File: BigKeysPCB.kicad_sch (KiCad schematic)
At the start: 24 parts, among them SW1 SW_Push, U1 ATmega32U4-M, Y1 16MHz

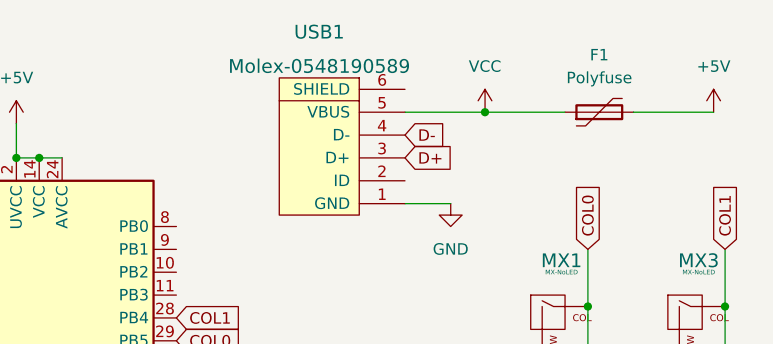
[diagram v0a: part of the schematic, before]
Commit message: shield connected to ground, missing connection added to pcb file
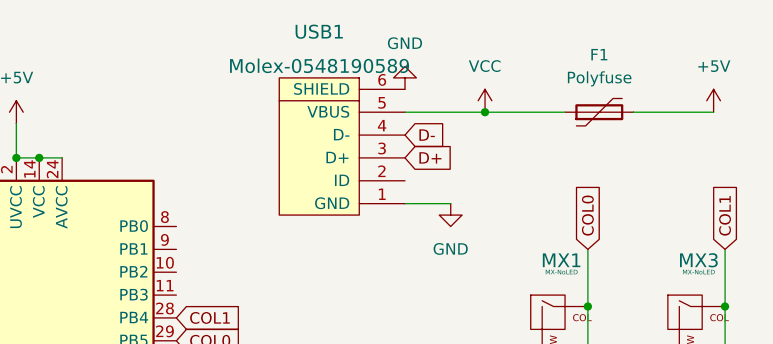
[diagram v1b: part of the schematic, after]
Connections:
- net GND: now also USB1.6 (SHIELD)
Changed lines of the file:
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@@
+    (pin "1")
+  )
+  (symbol (lib_id "power:GND") (at 186.69 33.02 180) (unit 1)
+    (in_bom yes) (on_board yes) (fields_autoplaced)
+    (property "Reference" "#PWR?" (id 0) (at 186.69 26.67 0)
+      (effects (font (size 1.27 1.27)) hide)
+    )
+    (property "Value" "GND" (id 1) (at 186.69 27.94 0))
+    (property "Footprint" "" (id 2) (at 186.69 33.02 0)
+      (effects (font (size 1.27 1.27)) hide)
+    )
+    (property "Datasheet" "" (id 3) (at 186.69 33.02 0)
+      (effects (font (size 1.27 1.27)) hide)
+    )
     (pin "1")
   )
@@
       (reference "#PWR0113") (unit 1) (value "GND") (footprint "")
     )
+    (path "/f978a9e3-d358-453b-a3d0-a4e6d5ba20c8"
+      (reference "#PWR?") (unit 1) (value "GND") (footprint "")
+    )
     (path "/93252823-c104-4d29-80b4-3fb6d71f8564"
